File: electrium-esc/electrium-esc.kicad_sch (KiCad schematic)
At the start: 0 parts

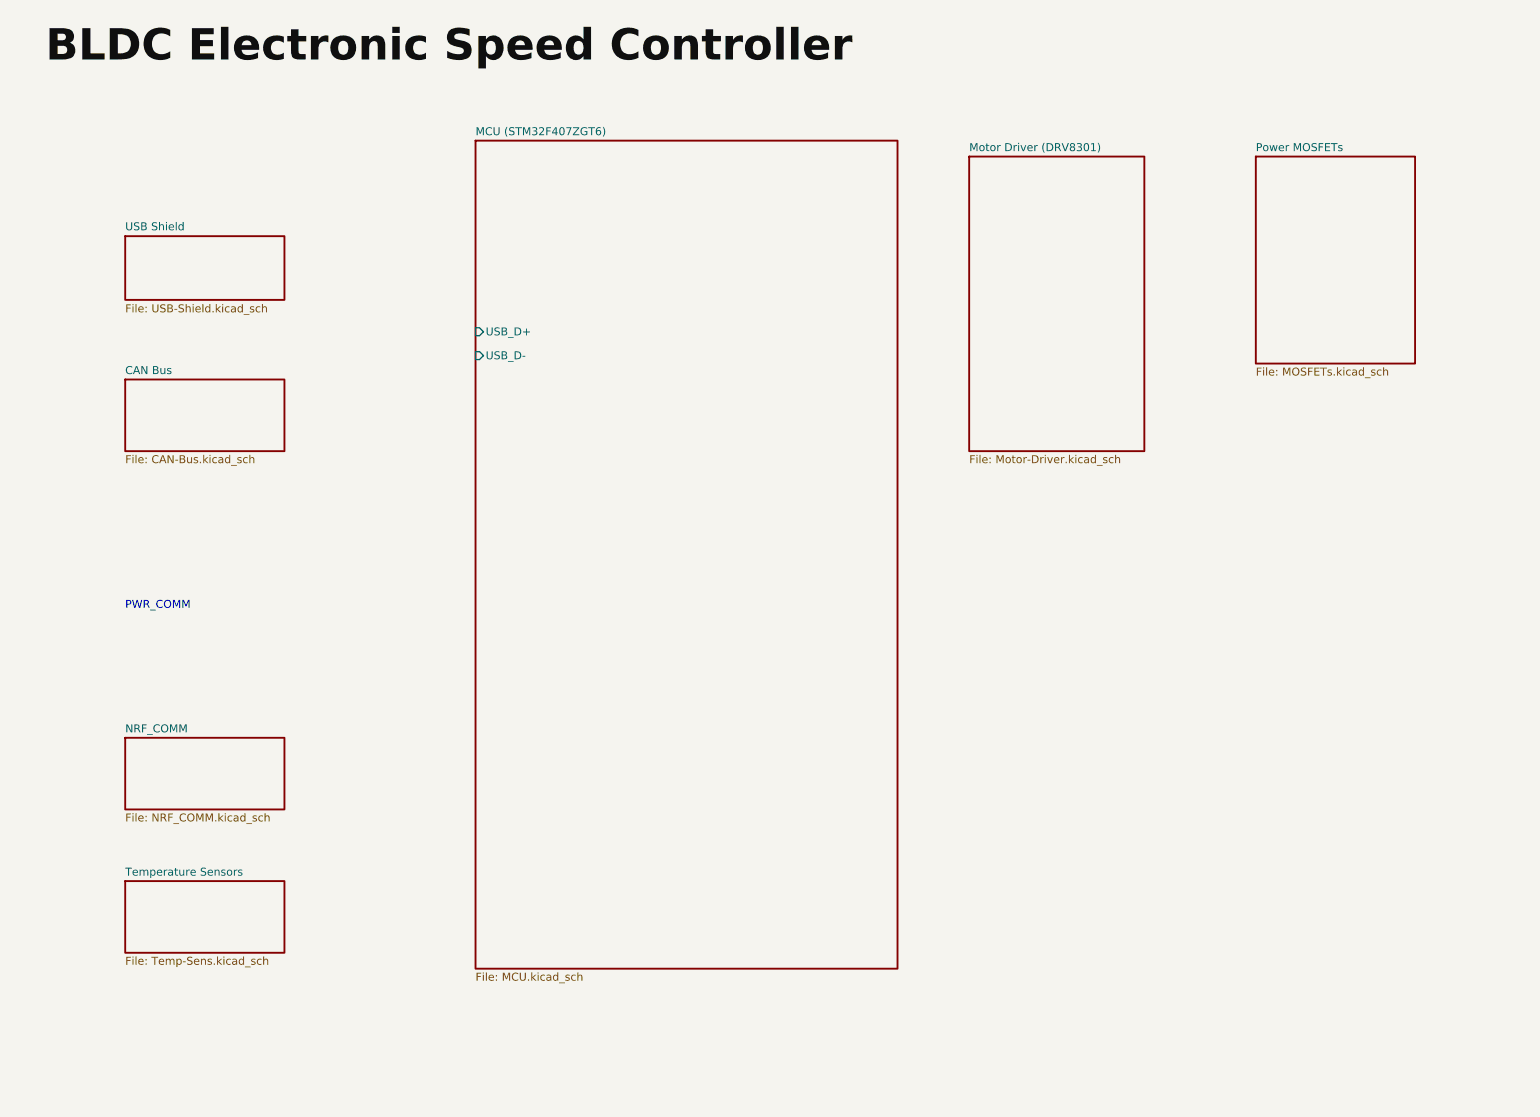
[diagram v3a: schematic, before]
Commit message: Add additional connections to MCU
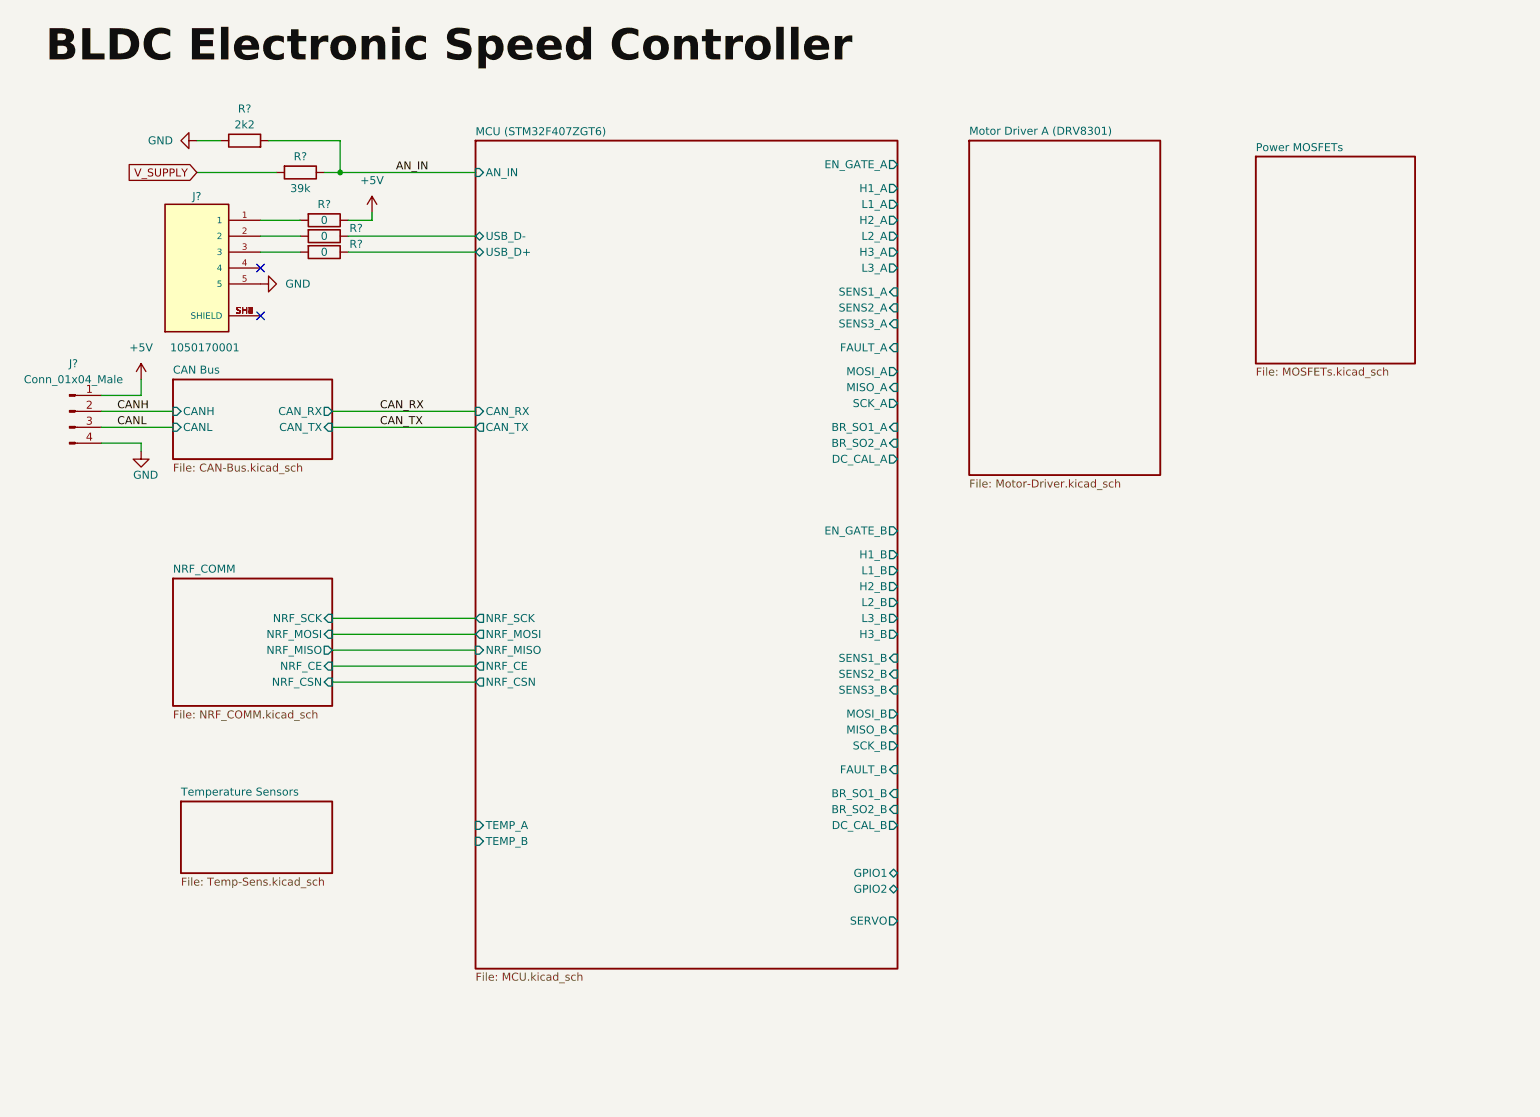
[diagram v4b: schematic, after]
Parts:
- added J?: Conn_01x04_Male, symbol Connector:Conn_01x04_Male
- added J?: 1050170001, MOLEX_1050170001, symbol 1050170001:1050170001
- added R?: 39k, symbol Device:R
- added R? (x3): 0, symbol Device:R
- added R?: 2k2, symbol Device:R
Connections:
- net MCU (STM32F407ZGT6)/USB_D+: now also R?.1
- net MCU (STM32F407ZGT6)/USB_D-: now also R?.1
- new net: J?.3, R?.2
- new net: J?.1, R?.2
- new net: J?.2, R?.2
- new net: J?.SH1 (SHIELD), J?.SH2 (SHIELD), J?.SH3 (SHIELD), J?.SH4 (SHIELD), J?.SH5 (SHIELD), J?.SH6 (SHIELD), J?.SH7 (SHIELD), J?.SH8 (SHIELD)
- new net +5V: J?.1 (Pin_1), R?.1
- new net AN_IN: R?.1, R?.2
- new net CANH: J?.2 (Pin_2)
- new net CANL: J?.3 (Pin_3)
- new net GND: J?.4 (Pin_4), J?.5, R?.1
- new net V_SUPPLY: R?.2
- no-connect marks 0 -> 2
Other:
- sheet Motor Driver (DRV8301) renamed Motor Driver A (DRV8301)
- removed sheet USB Shield
- sheet CAN Bus ports: added CANH, CANL, CAN_RX, CAN_TX; removed none
- sheet MCU (STM32F407ZGT6) ports: added AN_IN, BR_SO1_A, BR_SO1_B, BR_SO2_A, BR_SO2_B, CAN_RX, CAN_TX, DC_CAL_A, DC_CAL_B, EN_GATE_A, EN_GATE_B, FAULT_A, FAULT_B, GPIO1, GPIO2, H1_A, H1_B, H2_A, H2_B, H3_A, H3_B, L1_A, L1_B, L2_A, L2_B, L3_A, L3_B, MISO_A, MISO_B, MOSI_A, MOSI_B, NRF_CE, NRF_CSN, NRF_MISO, NRF_MOSI, NRF_SCK, SCK_A, SCK_B, SENS1_A, SENS1_B, SENS2_A, SENS2_B, SENS3_A, SENS3_B, SERVO, TEMP_A, TEMP_B; removed none
- sheet NRF_COMM ports: added NRF_CE, NRF_CSN, NRF_MISO, NRF_MOSI, NRF_SCK; removed none
- note removed: "PWR_COMM"

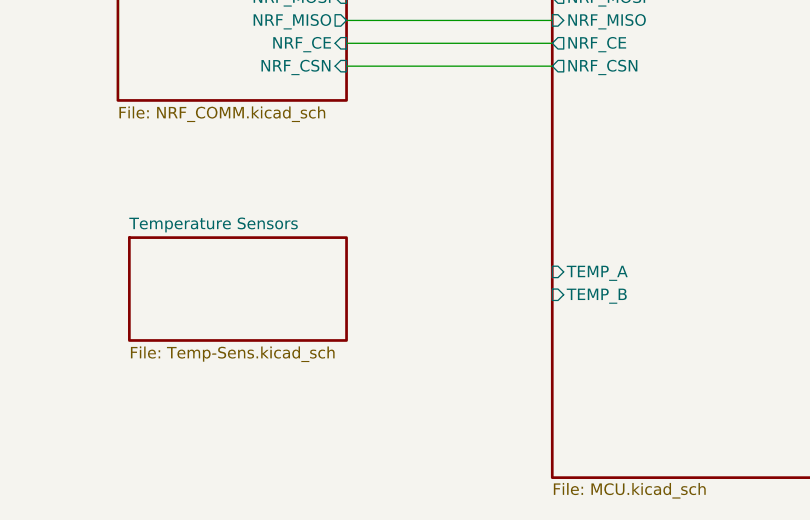
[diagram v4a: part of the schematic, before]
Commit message: Connect Temperature Sensors
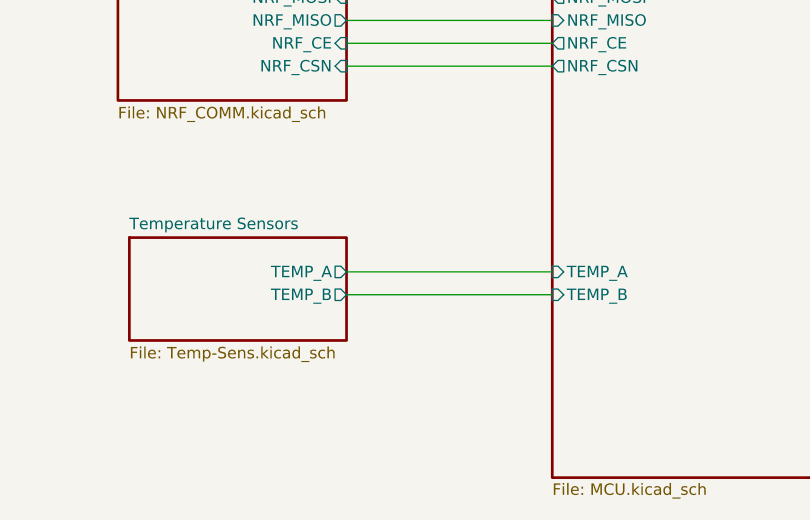
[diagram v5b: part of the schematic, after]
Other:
- sheet Temperature Sensors ports: added TEMP_A, TEMP_B; removed none
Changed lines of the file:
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@@
+    (stroke (width 0) (type default) (color 0 0 0 0))
+  )
+  (wire (pts (xy 64.77 147.32) (xy 87.63 147.32))
     (stroke (width 0) (type default) (color 0 0 0 0))
   )
   (wire (pts (xy 66.04 38.1) (xy 54.61 38.1))
+    (stroke (width 0) (type default) (color 0 0 0 0))
+  )
+  (wire (pts (xy 64.77 149.86) (xy 87.63 149.86))
     (stroke (width 0) (type default) (color 0 0 0 0))
   )
@@
       (effects (font (size 1.27 1.27)) (justify left top))
     )
+    (pin "TEMP_A" output (at 64.77 147.32 0)
+      (effects (font (size 1.27 1.27)) (justify right))
+    )
+    (pin "TEMP_B" output (at 64.77 149.86 0)
+      (effects (font (size 1.27 1.27)) (justify right))
+    )
   )
   (sheet (at 39.37 76.2) (size 25.4 12.7) (fields_autoplaced)
@@
       (reference "#PWR?") (unit 1) (value "GND") (footprint "")
     )
+    (path "/d8de0f32-7506-49aa-9adf-28277e02e6ca/2972fae5-cfef-4ccb-b80f-9f059b848566"
+      (reference "#PWR?") (unit 1) (value "GND") (footprint "")
+    )
     (path "/f169605c-998e-4bf3-977e-b281c665fab8/2ee81e03-2f9f-4feb-8cfe-725c69becd84"
       (reference "#PWR?") (unit 1) (value "GND") (footprint "")
@@
       (reference "#PWR?") (unit 1) (value "GND") (footprint "")
     )
+    (path "/d8de0f32-7506-49aa-9adf-28277e02e6ca/b7bb838f-03b3-4711-b1c9-755b1d4c0747"
+      (reference "#PWR?") (unit 1) (value "GND") (footprint "")
+    )
     (path "/95515899-f309-4706-b478-ef0c1d74de3d/b86fe26a-3f99-4537-9f2f-6dd47cea0948"
       (reference "#PWR?") (unit 1) (value "+3.3V") (footprint "")
@@
       (reference "#PWR?") (unit 1) (value "GND") (footprint "")
     )
+    (path "/d8de0f32-7506-49aa-9adf-28277e02e6ca/c8e4bfc3-cd0a-4858-be68-31329663b00c"
+      (reference "#PWR?") (unit 1) (value "+3.3V") (footprint "")
+    )
     (path "/95515899-f309-4706-b478-ef0c1d74de3d/cd67e38c-7d04-4cf1-9a05-b2a617aae454"
       (reference "#PWR?") (unit 1) (value "GND") (footprint "")
@@
     (path "/d6be1da7-7790-4ae3-a0f4-2b23be7f9c03"
       (reference "#PWR?") (unit 1) (value "GND") (footprint "")
+    )
+    (path "/d8de0f32-7506-49aa-9adf-28277e02e6ca/e4810854-05f6-4f63-85cf-ee0c3bd9e57f"
+      (reference "#PWR?") (unit 1) (value "+3.3V") (footprint "")
     )
     (path "/4dcd2554-0c0c-4fca-b220-d2fb156d9cf9/f08bab5d-4585-46c6-86fb-037f9e85b871"
@@
       (reference "R?") (unit 1) (value "0") (footprint "")
     )
+    (path "/d8de0f32-7506-49aa-9adf-28277e02e6ca/a9edeece-3a26-415f-9016-4bc6c3332636"
+      (reference "R?") (unit 1) (value "10k") (footprint "")
+    )
     (path "/4dcd2554-0c0c-4fca-b220-d2fb156d9cf9/b40e4240-9146-4636-b31a-fe7829791e9e"
       (reference "R?") (unit 1) (value "100") (footprint "")
@@
       (reference "R?") (unit 1) (value "IN") (footprint "")
     )
+    (path "/d8de0f32-7506-49aa-9adf-28277e02e6ca/ff5c54f7-2db5-4e8c-bf21-9ccaa8e0a1bf"
+      (reference "R?") (unit 1) (value "10k") (footprint "")
+    )
     (path "/4dcd2554-0c0c-4fca-b220-d2fb156d9cf9/fffaf85d-0ec3-47a5-a0c2-5dee4f447c44"

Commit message: Modify title
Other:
- note added: "BLDC Electronic Speed Controller"
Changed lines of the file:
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@@
     (stroke (width 0) (type default) (color 0 0 0 0))
+  )
+  (text "BLDC Electronic Speed Controller" (at 21.59 26.67 0)
+    (effects (font (size 5 5) (thickness 1) bold) (justify left bottom))
   )
   (label "AN_IN" (at 74.93 43.18 0)
@@
   (label "CANL" (at 30.48 83.82 0)
     (effects (font (size 1.27 1.27)) (justify left bottom))
-  )
-  (label "BLDC Electronic Speed Controller" (at 19.05 26.67 0)
-    (effects (font (size 5 5) (thickness 1) bold) (justify left bottom))
   )
   (global_label "V_SUPPLY" (shape input) (at 43.18 43.18 180) (fields_autoplaced)
@@
       (reference "#PWR?") (unit 1) (value "+3.3V") (footprint "")
     )
+    (path "/95515899-f309-4706-b478-ef0c1d74de3d/3f68030b-6d3f-42b1-bf5c-b4480d490aeb"
+      (reference "#PWR?") (unit 1) (value "GND") (footprint "")
+    )
     (path "/95515899-f309-4706-b478-ef0c1d74de3d/40bb8d27-a5fc-4ad9-9dfd-9671646352b1"
       (reference "#PWR?") (unit 1) (value "GND") (footprint "")
     )
     (path "/95515899-f309-4706-b478-ef0c1d74de3d/4a9efcc8-e7ec-4e3a-8761-49cbbf48d098"
+      (reference "#PWR?") (unit 1) (value "GND") (footprint "")
+    )
+    (path "/95515899-f309-4706-b478-ef0c1d74de3d/4d04a725-4fac-46d9-bc06-451f3efb84bf"
       (reference "#PWR?") (unit 1) (value "GND") (footprint "")
     )
@@
       (reference "#PWR?") (unit 1) (value "GND") (footprint "")
     )
+    (path "/95515899-f309-4706-b478-ef0c1d74de3d/6f0ae85c-195e-461d-9670-d565880d2131"
+      (reference "#PWR?") (unit 1) (value "+3.3V") (footprint "")
+    )
     (path "/95515899-f309-4706-b478-ef0c1d74de3d/7435bdad-b836-48fc-b0eb-27c0810133d2"
       (reference "#PWR?") (unit 1) (value "+3.3V") (footprint "")
@@
       (reference "#PWR?") (unit 1) (value "GND") (footprint "")
     )
+    (path "/95515899-f309-4706-b478-ef0c1d74de3d/c2f685c3-fe59-4928-a1f2-65e58314f27b"
+      (reference "#PWR?") (unit 1) (value "+5V") (footprint "")
+    )
     (path "/d8de0f32-7506-49aa-9adf-28277e02e6ca/c8e4bfc3-cd0a-4858-be68-31329663b00c"
       (reference "#PWR?") (unit 1) (value "+3.3V") (footprint "")
@@
       (reference "C?") (unit 1) (value "1u") (footprint "")
     )
+    (path "/95515899-f309-4706-b478-ef0c1d74de3d/3947b609-11a8-4126-9e3a-a7f0be9bfca0"
+      (reference "C?") (unit 1) (value "2.2u") (footprint "")
+    )
     (path "/95515899-f309-4706-b478-ef0c1d74de3d/39c07361-b640-4cc9-b641-4c943a6af412"
       (reference "C?") (unit 1) (value "100n") (footprint "")
@@
       (reference "C?") (unit 1) (value "4.7u") (footprint "")
     )
+    (path "/95515899-f309-4706-b478-ef0c1d74de3d/7116efe9-7606-4a69-ac80-f537cdc4bd52"
+      (reference "C?") (unit 1) (value "2.2u") (footprint "")
+    )
     (path "/4dcd2554-0c0c-4fca-b220-d2fb156d9cf9/72b22397-6364-471b-86f4-98c684f0c349"
       (reference "C?") (unit 1) (value "15u") (footprint "")
@@
       (reference "C?") (unit 1) (value "0.1u") (footprint "")
     )
+    (path "/d8de0f32-7506-49aa-9adf-28277e02e6ca/ab14ddb5-b4d3-44b9-95bd-3a200aa62a0f"
+      (reference "C?") (unit 1) (value "2.2u") (footprint "")
+    )
     (path "/95515899-f309-4706-b478-ef0c1d74de3d/aea6117c-6556-4b30-acf0-e2d7985fe373"
       (reference "C?") (unit 1) (value "100n") (footprint "")
@@
       (reference "C?") (unit 1) (value "100n") (footprint "")
     )
+    (path "/d8de0f32-7506-49aa-9adf-28277e02e6ca/e6b54195-98b5-4b4f-a72e-f268fef27886"
+      (reference "C?") (unit 1) (value "2.2u") (footprint "")
+    )
     (path "/4dcd2554-0c0c-4fca-b220-d2fb156d9cf9/ec717b4f-d633-4eec-b5ad-76aabfa00474"
       (reference "C?") (unit 1) (value "120p") (footprint "")
@@
       (reference "L?") (unit 1) (value "22u") (footprint "")
     )
+    (path "/95515899-f309-4706-b478-ef0c1d74de3d/764763fd-5dd9-4c52-a8c3-a0c0d2fc9a51"
+      (reference "PS?") (unit 1) (value "TC2117-3.3VDBTR") (footprint "SOT230P700X180-4N")
+    )
     (path "/4dcd2554-0c0c-4fca-b220-d2fb156d9cf9/16e0dec1-cd59-4265-ae93-70fdea2366c6"

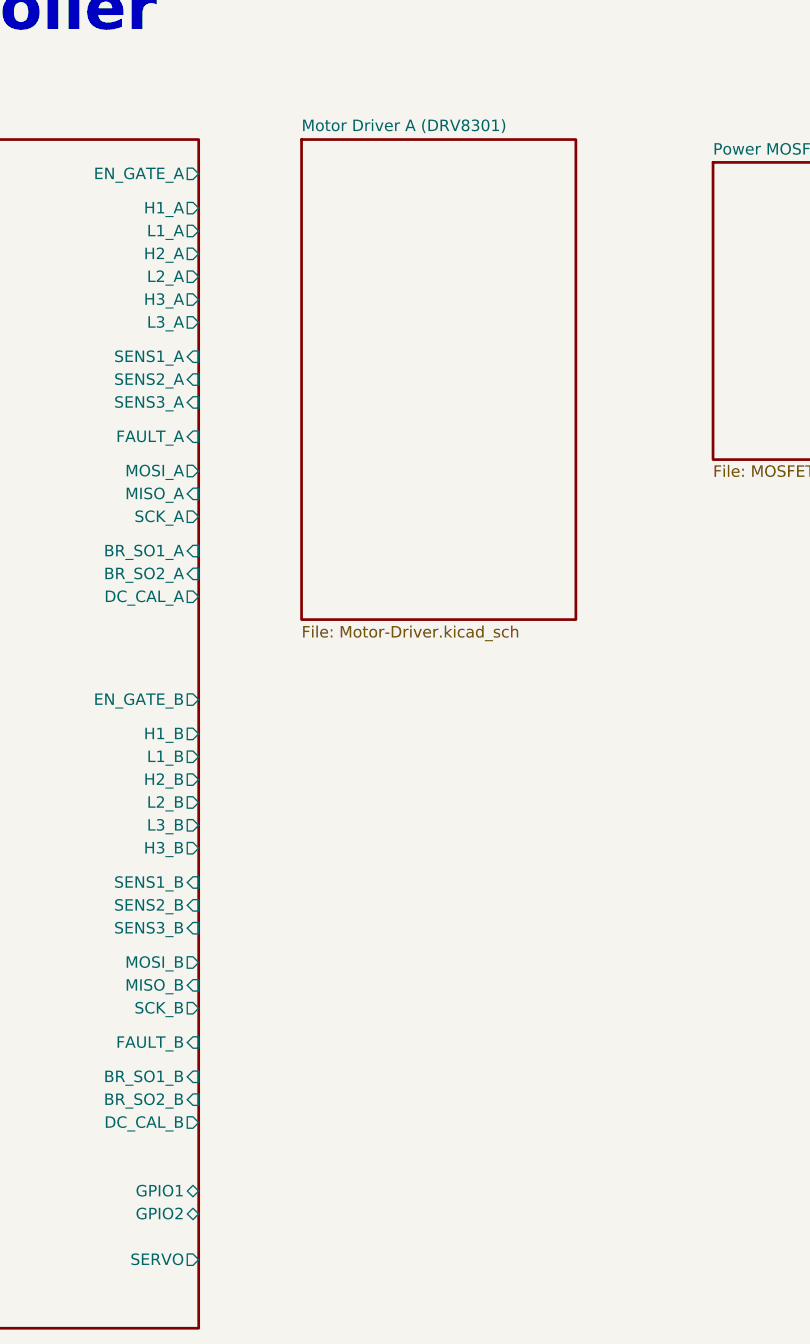
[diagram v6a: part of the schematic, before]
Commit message: Add files via upload
MCU->Driver
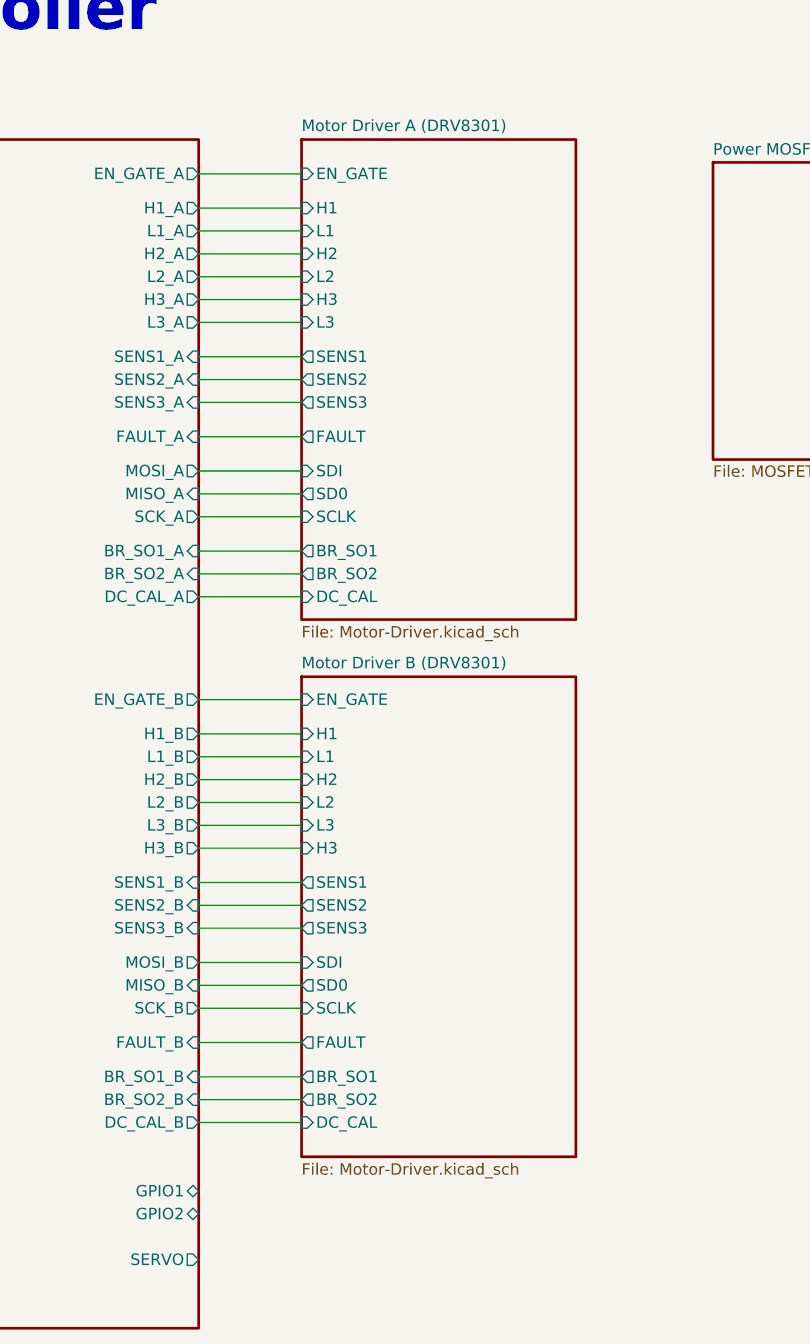
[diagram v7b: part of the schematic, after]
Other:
- added sheet Motor Driver B (DRV8301) (Motor-Driver.kicad_sch)
- sheet Motor Driver A (DRV8301) ports: added BR_SO1, BR_SO2, DC_CAL, EN_GATE, FAULT, H1, H2, H3, L1, L2, L3, SCLK, SD0, SDI, SENS1, SENS2, SENS3; removed none
